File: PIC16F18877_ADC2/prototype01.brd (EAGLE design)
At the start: 95 x 72 mm, 39 parts, among them CN1 12V_IN, CN10 PIC_PORTD_IF, CN2 PIC_PORTA_IF, CN3 UART_IF, CN4 PIC_CN_H, CN5 AE-MICRO-SD-DIP, CN6 I2C_IF, CN7 PIC_PORTB_IF, CN8 PIC_PORTE_IF, CN9 PIC_PORTC_IF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

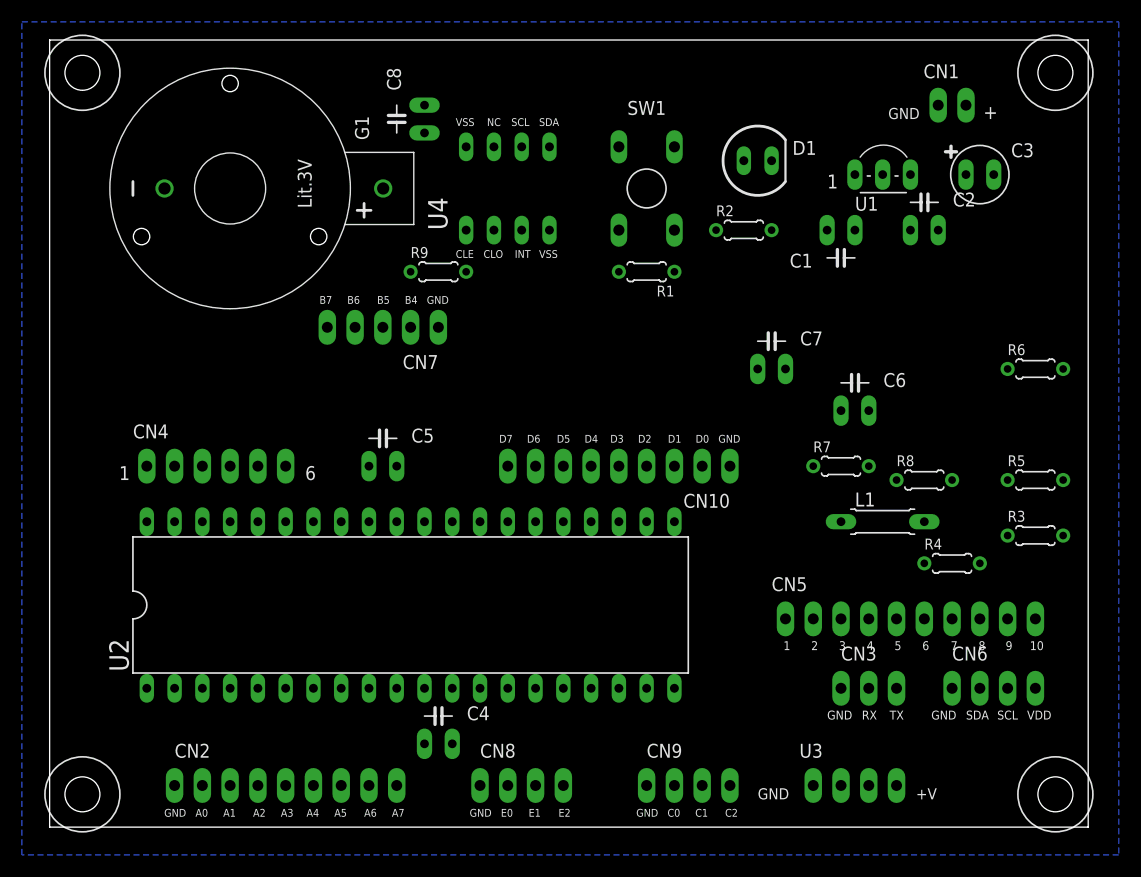
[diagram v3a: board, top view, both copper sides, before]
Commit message: 部品配置を修正
SDスロット、液晶ディスプレイなどの配置を考慮し、大幅に見直し
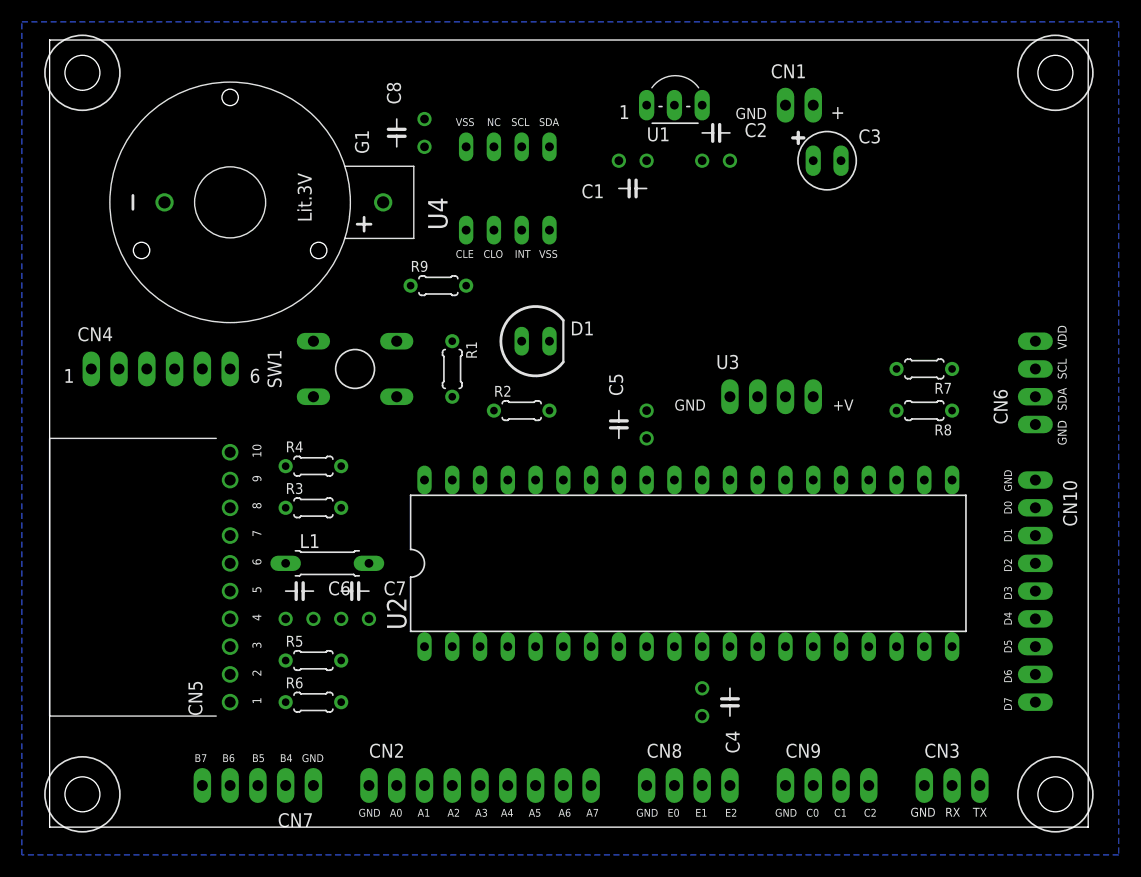
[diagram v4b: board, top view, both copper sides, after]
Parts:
- moved R6 72.7 mm to (24.1, 11.4)
- moved R5 68.1 mm to (24.1, 15.2)
- moved R3 66.1 mm to (24.1, 29.2)
- moved R4 59.1 mm to (24.1, 33.0)
- moved C6 54.3 mm to (22.9, 19.1)
- moved L1 50.9 mm to (21.6, 24.1)
- moved CN5 50.3 mm to (17.8, 10.2), turned to 90 degrees
- moved C7 44.4 mm to (27.9, 19.1)
- moved CN7 43.4 mm to (24.1, 3.81)
- moved U3 36.4 mm to (62.2, 39.4)
- moved CN10 28.0 mm to (90.2, 31.8), turned to 270 degrees
- moved SW1 27.4 mm to (31.8, 44.5), turned to 270 degrees
- moved R2 26.2 mm to (43.2, 38.1)
- moved D1 26.2 mm to (44.5, 44.5)
- moved U2 25.7 mm to (58.4, 24.1)
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
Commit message: 部品配置を修正
液晶ディスプレイの外形による見直し発生
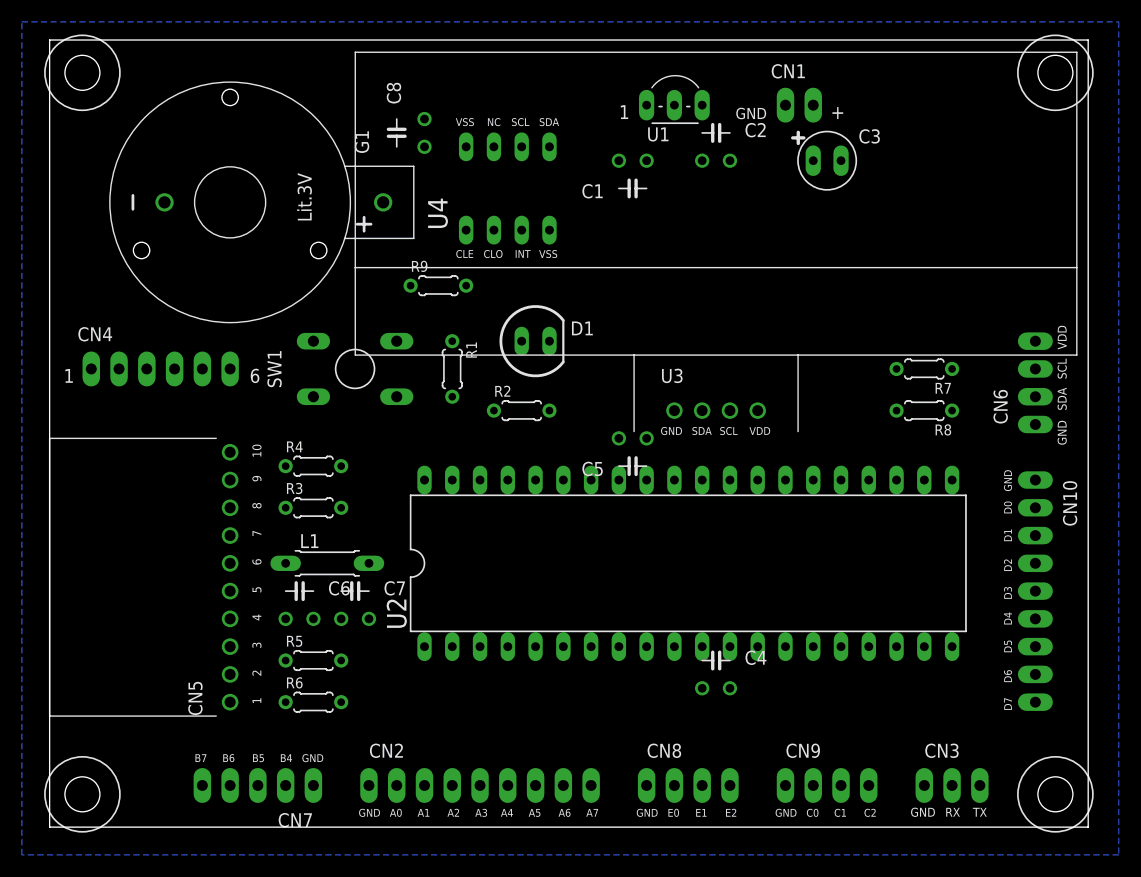
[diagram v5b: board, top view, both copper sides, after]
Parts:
- moved U3 5.24 mm to (57.1, 38.1)
- moved C4 1.80 mm to (61.0, 12.7), turned to 0 degrees
- moved C5 1.80 mm to (53.3, 35.6), turned to 180 degrees
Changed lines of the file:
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@@
 <element name="C2" library="Parts" package="CAP_100MIL" value="1uF" x="60.96" y="60.96"/>
 <element name="C3" library="Parts" package="ELECAP_D5_100MIL" value="10uF" x="71.12" y="60.96"/>
-<element name="C4" library="Parts" package="CAP_100MIL" value="0.1uF" x="59.69" y="11.43" rot="R270"/>
-<element name="C5" library="Parts" package="CAP_100MIL" value="0.1uF" x="54.61" y="36.83" rot="R90"/>
+<element name="C4" library="Parts" package="CAP_100MIL" value="0.1uF" x="60.96" y="12.7"/>
+<element name="C5" library="Parts" package="CAP_100MIL" value="0.1uF" x="53.34" y="35.56" rot="R180"/>
 <element name="C6" library="Parts" package="CAP_100MIL" value="10uF" x="22.86" y="19.05"/>
 <element name="C7" library="Parts" package="CAP_100MIL" value="0.1uF" x="27.94" y="19.05"/>
@@
 <element name="U1" library="Parts" package="TO92-LINE" value="XC6202P332TH" x="54.61" y="66.04"/>
 <element name="U2" library="Parts" package="DIL40" value="PIC16F18877-I/P" x="58.42" y="24.13"/>
-<element name="U3" library="PartsForProto" package="AE-AQM1602A" value="AE-AQM1602A" x="62.23" y="39.37"/>
+<element name="U3" library="PartsForProto" package="AE-AQM1602A" value="AE-AQM1602A" x="57.15" y="38.1"/>
 <element name="U4" library="PartsForProto" package="DIL8_AE-RTC-8564NB" value="AE-RTC-8564NB" x="38.1" y="54.61"/>
 </elements>
@@
 <contactref element="CN6" pad="3"/>
 <wire x1="82.55" y1="41.91" x2="90.17" y2="41.91" width="0" layer="19" extent="1-1"/>
-<wire x1="67.31" y1="39.37" x2="82.55" y2="41.91" width="0" layer="19" extent="1-1"/>
-<wire x1="77.47" y1="16.51" x2="67.31" y2="39.37" width="0" layer="19" extent="1-1"/>
-<wire x1="43.18" y1="62.23" x2="67.31" y2="39.37" width="0" layer="19" extent="1-1"/>
+<wire x1="62.23" y1="38.1" x2="82.55" y2="41.91" width="0" layer="19" extent="1-1"/>
+<wire x1="77.47" y1="16.51" x2="82.55" y2="41.91" width="0" layer="19" extent="1-1"/>
+<wire x1="43.18" y1="62.23" x2="62.23" y2="38.1" width="0" layer="19" extent="1-1"/>
 </signal>
 <signal name="SDA1">
@@
 <wire x1="82.55" y1="38.1" x2="90.17" y2="39.37" width="0" layer="19" extent="1-1"/>
 <wire x1="77.47" y1="31.75" x2="82.55" y2="38.1" width="0" layer="19" extent="1-1"/>
-<wire x1="64.77" y1="39.37" x2="77.47" y2="31.75" width="0" layer="19" extent="1-1"/>
-<wire x1="45.72" y1="62.23" x2="64.77" y2="39.37" width="0" layer="19" extent="1-1"/>
+<wire x1="59.69" y1="38.1" x2="77.47" y2="31.75" width="0" layer="19" extent="1-1"/>
+<wire x1="45.72" y1="62.23" x2="59.69" y2="38.1" width="0" layer="19" extent="1-1"/>
 </signal>
 <signal name="N$1">
@@
 <wire x1="77.47" y1="41.91" x2="90.17" y2="44.45" width="0" layer="19" extent="1-1"/>
 <wire x1="77.47" y1="38.1" x2="77.47" y2="41.91" width="0" layer="19" extent="1-1"/>
-<wire x1="69.85" y1="39.37" x2="77.47" y2="38.1" width="0" layer="19" extent="1-1"/>
-<wire x1="54.61" y1="35.56" x2="69.85" y2="39.37" width="0" layer="19" extent="1-1"/>
+<wire x1="64.77" y1="38.1" x2="77.47" y2="38.1" width="0" layer="19" extent="1-1"/>
+<wire x1="54.61" y1="35.56" x2="64.77" y2="38.1" width="0" layer="19" extent="1-1"/>
 <wire x1="54.61" y1="31.75" x2="54.61" y2="35.56" width="0" layer="19" extent="1-1"/>
 <wire x1="59.69" y1="16.51" x2="54.61" y2="31.75" width="0" layer="19" extent="1-1"/>
@@
 <wire x1="36.83" y1="39.37" x2="54.61" y2="35.56" width="0" layer="19" extent="1-1"/>
 <wire x1="29.21" y1="24.13" x2="36.83" y2="39.37" width="0" layer="19" extent="1-1"/>
-<wire x1="54.61" y1="60.96" x2="54.61" y2="35.56" width="0" layer="19" extent="1-1"/>
+<wire x1="54.61" y1="60.96" x2="64.77" y2="38.1" width="0" layer="19" extent="1-1"/>
 <wire x1="54.61" y1="66.04" x2="54.61" y2="60.96" width="0" layer="19" extent="1-1"/>
 <wire x1="6.35" y1="41.91" x2="29.21" y2="24.13" width="0" layer="19" extent="1-1"/>

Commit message: 部品配置を修正
LEDの位置をピンのそばに移動
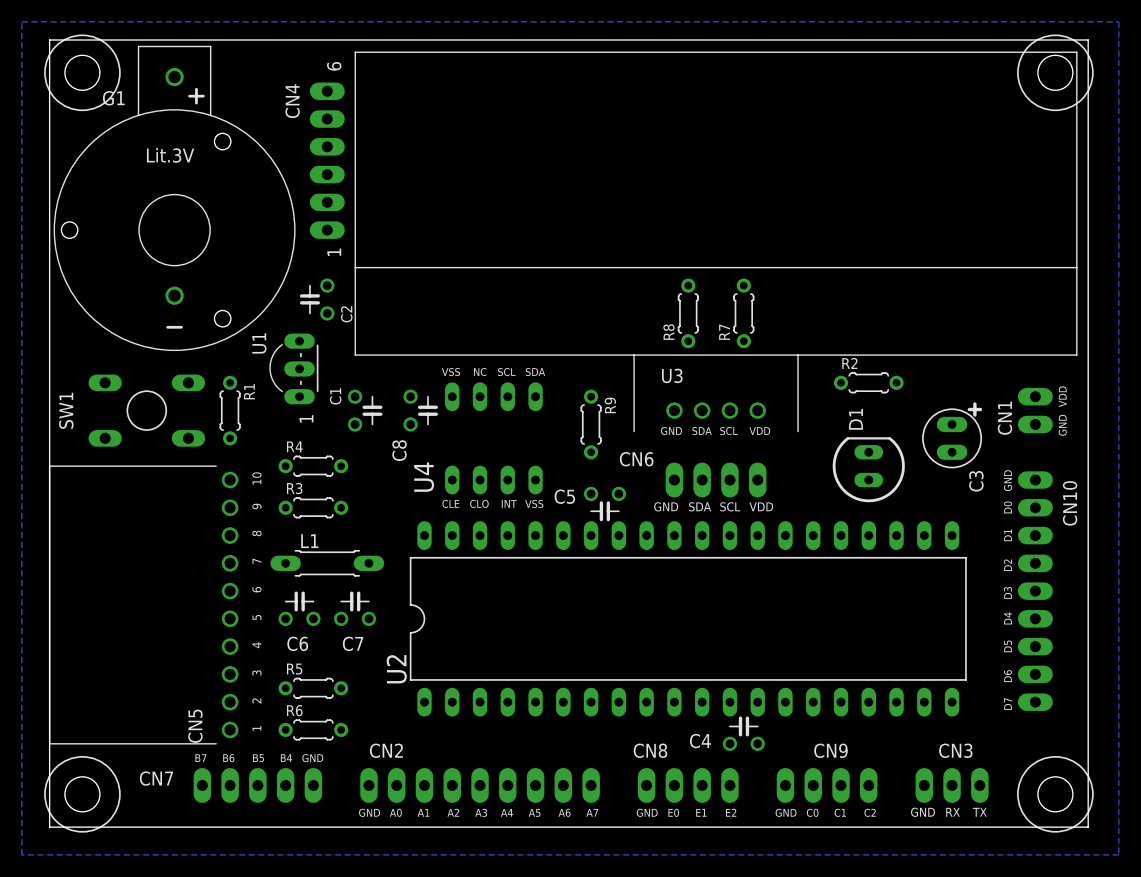
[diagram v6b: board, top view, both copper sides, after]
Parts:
- moved U1 41.5 mm to (22.9, 39.4), turned to 90 degrees
- moved C2 37.8 mm to (25.4, 48.3), turned to 90 degrees
- moved CN1 37.1 mm to (90.2, 36.8), turned to 90 degrees
- moved C1 34.2 mm to (27.9, 38.1), turned to 270 degrees
- moved CN6 33.4 mm to (57.1, 31.8), turned to 0 degrees
- moved D1 32.6 mm to (74.9, 33.0), turned to 90 degrees
- moved R2 31.9 mm to (74.9, 40.6)
- moved C3 27.9 mm to (82.5, 35.6), turned to 270 degrees
- moved C8 25.4 mm to (33.0, 38.1), turned to 270 degrees
- moved CN4 25.0 mm to (25.4, 54.6), turned to 90 degrees
- moved R8 23.3 mm to (58.4, 47.0), turned to 90 degrees
- moved U4 22.9 mm to (36.8, 31.8)
- moved R1 20.7 mm to (16.5, 38.1)
- moved SW1 19.4 mm to (12.7, 40.6)
- moved R9 18.9 mm to (49.5, 36.8), turned to 270 degrees
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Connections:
- removed net N$20: U2.19
- removed net N$21: U2.20
- net RD0: now also U2.19
- net RD1: now also U2.20

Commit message: 部品配置を修正
LCD、RTCC周辺の部品配置を見直し
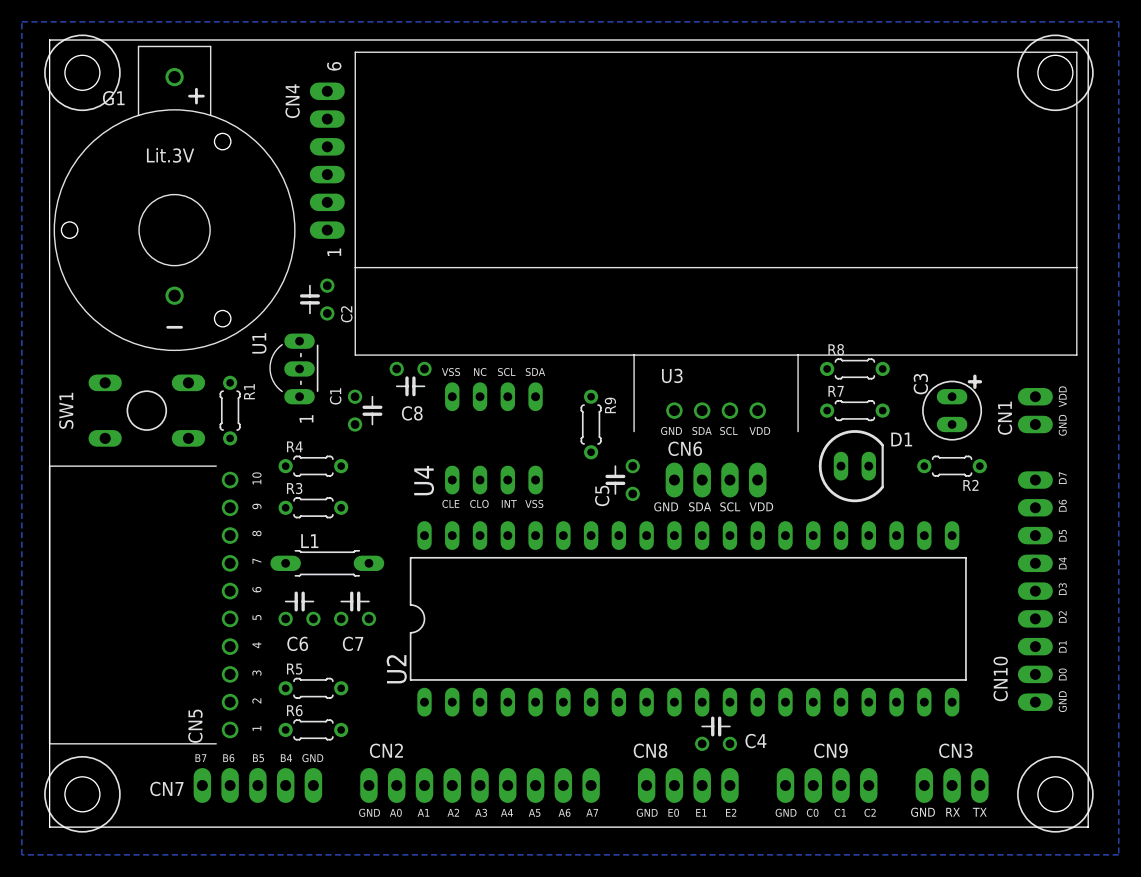
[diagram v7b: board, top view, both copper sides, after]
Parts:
- moved CN10 20.3 mm to (90.2, 11.4), turned to 90 degrees
- moved R8 16.1 mm to (73.7, 41.9), turned to 0 degrees
- moved R7 13.5 mm to (73.7, 38.1), turned to 0 degrees
- moved R2 10.8 mm to (82.5, 33.0), turned to 180 degrees
- moved C8 3.81 mm to (33.0, 41.9), turned to 180 degrees
- moved C5 2.84 mm to (53.3, 31.8), turned to 90 degrees
- moved C3 2.54 mm to (82.5, 38.1)
- moved C4 2.54 mm to (61.0, 7.62)
- moved D1 1.27 mm to (73.7, 33.0), turned to 0 degrees
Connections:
- net 0V: now also SW1.1; no longer SW1.4
- net N$3: now also SW1.4; no longer SW1.1

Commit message: 配線作業
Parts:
- turned R1 to 90 degrees
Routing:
- net +3V3: track 0.00 -> 117.8 mm
- net N$3: track 0.00 -> 106.5 mm
- net SDA1: track 0.00 -> 55.3 mm
- net +3V: track 0.00 -> 54.1 mm
- net N$4: track 0.00 -> 43.8 mm
- net N$2: track 0.00 -> 39.8 mm
- net N$9: track 0.00 -> 39.7 mm
- net RA6: track 0.00 -> 31.5 mm
- net UART_RX: track 0.00 -> 28.1 mm
- net UART_TX: track 0.00 -> 28.1 mm, vias 0 -> 1
- net RA7: track 0.00 -> 25.8 mm
- net +12V: track 0.00 -> 22.0 mm
- net RD1: track 0.00 -> 20.2 mm
- net SCL1: track 0.00 -> 17.4 mm
- net RD3: track 0.00 -> 16.1 mm
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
